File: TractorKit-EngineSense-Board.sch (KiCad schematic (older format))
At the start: 24 parts

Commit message: Final schematic
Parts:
- gave numbers to parts that had none: 24

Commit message: Final 2
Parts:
- added R10, R11, R12, R13, R9: 1k, Resistor_THT:R_Axial_DIN0207_L6.3mm_D2.5mm_P10.16mm_Horizontal, symbol Device:R
- added R4, R5, R6, R7, R8: 10k, Resistor_THT:R_Axial_DIN0207_L6.3mm_D2.5mm_P10.16mm_Horizontal, symbol Device:R
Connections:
- net +12V: now also J2.3 (Pin_3)
- net GND: now also R10.2, R11.2, R12.2, R13.2, R9.2
- net at J2.1 (Pin_1): now also R7.1
- net at J2.2 (Pin_2): now also R8.1
- net at J3.1 (Pin_1): now also R4.1
- net at J3.2 (Pin_2): now also R5.1
- net at J3.3 (Pin_3): now also R6.1
- net RX: now reaches J4.1 (Pin_1)
- net RX: now also U3.27 (IO16)
- net TX: now reaches J4.2 (Pin_2)
- net TX: now also U3.28 (IO17)
- net at U3.10 (IO25): now also R4.2, R9.1
- net at U3.11 (IO26): now also R10.1, R5.2
- net at U3.12 (IO27): now also R11.1, R6.2
- net at U3.7 (IO35): now also R13.1, R8.2
- net at U3.8 (IO32): now also R12.1, R7.2
- no-connect marks 8 -> 19
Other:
- note added: "12V WITH\nCURRENT\nSENSING"
- moved on the sheet: J2, J3, J4, J5

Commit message: First complete draft.
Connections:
- net ADC1_4: now reaches J2.1 (Pin_1), R7.1
- net ADC1_7: now reaches J2.2 (Pin_2), R8.1
- net ADC2_8: now reaches J3.1 (Pin_1), R4.1
- net ADC2_9: now reaches J3.2 (Pin_2), R5.1
- net ADC2_7: now reaches J3.3 (Pin_3), R6.1
- net 12VIN: now reaches J1.1 (Pin_1), JP1.2 (B), R1.1, U2.1 (IP+), U2.2 (IP+)
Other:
- moved on the sheet: R10, R11, R12, R13, R4, R5, R6, R7, R8, R9

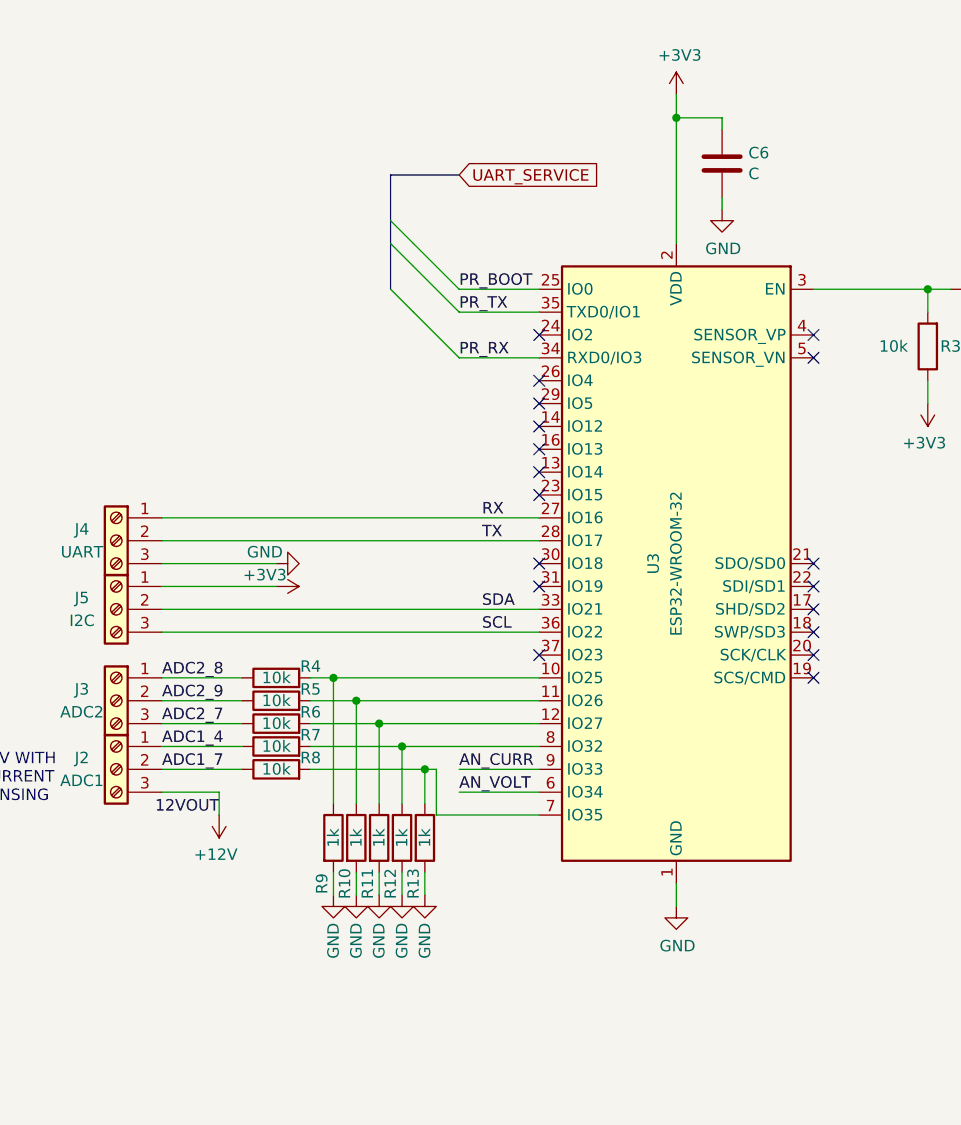
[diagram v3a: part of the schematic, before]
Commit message: Moved to SMD components
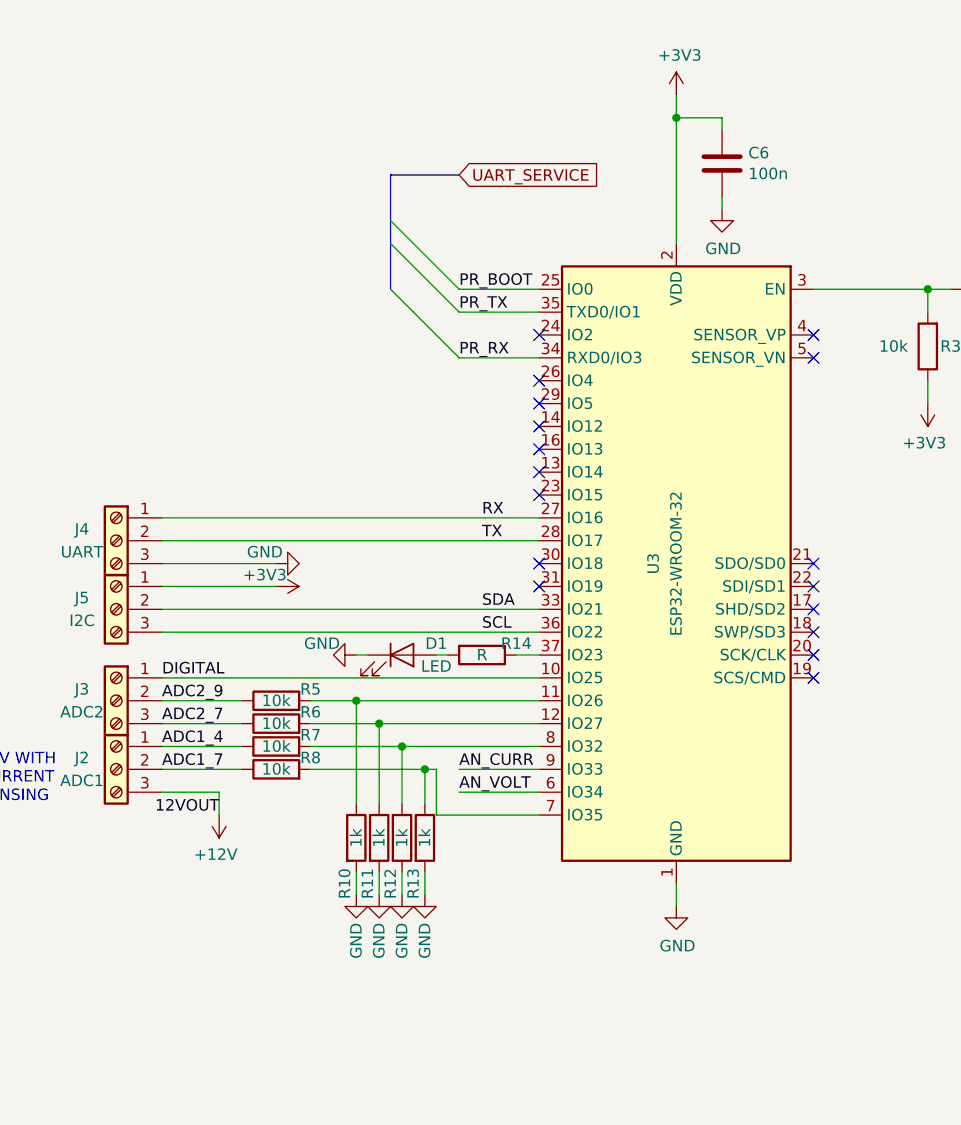
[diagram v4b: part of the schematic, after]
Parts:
- removed R4: 10k, Resistor_THT:R_Axial_DIN0207_L6.3mm_D2.5mm_P10.16mm_Horizontal, symbol Device:R
- removed R9: 1k, Resistor_THT:R_Axial_DIN0207_L6.3mm_D2.5mm_P10.16mm_Horizontal, symbol Device:R
- added D1: LED, LED_SMD:LED_0603_1608Metric_Pad1.05x0.95mm_HandSolder, symbol Device:LED
- added R14: R, Resistor_SMD:R_0603_1608Metric_Pad1.05x0.95mm_HandSolder, symbol Device:R
- C6: value C -> 100n
- R1, R10, R11, R12, R13, R2, R3, R5, R6, R7, R8: footprint Resistor_THT:R_Axial_DIN0207_L6.3mm_D2.5mm_P10.16mm_Horizontal -> Resistor_SMD:R_0603_1608Metric_Pad1.05x0.95mm_HandSolder
- TP1, TP2, TP3, TP4, TP5: footprint TestPoint:TestPoint_Pad_D1.5mm -> TestPoint:TestPoint_Pad_D1.0mm
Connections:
- net ADC2_8 is gone; now on net DIGITAL: J3.1 (Pin_1)
- net GND: now also D1.1 (K)
- net DIGITAL: now reaches U3.10 (IO25)
- net at U3.37 (IO23): now also R14.1
- new net: D1.2 (A), R14.2
- no-connect marks 19 -> 18
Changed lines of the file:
@@
 F 0 "TP5" V 2150 7150 50  0000 L CNN
 F 1 "SERVICE_GND" V 2150 7350 50  0000 L CNN
-F 2 "TestPoint:TestPoint_Pad_D1.5mm" H 2350 6950 50  0001 C CNN
+F 2 "TestPoint:TestPoint_Pad_D1.0mm" H 2350 6950 50  0001 C CNN
 F 3 "~" H 2350 6950 50  0001 C CNN
 	1    2150 6950
@@
 F 0 "TP3" V 2150 6950 50  0000 L CNN
 F 1 "SERVICE_RX" V 2150 7150 50  0000 L CNN
-F 2 "TestPoint:TestPoint_Pad_D1.5mm" H 2350 6750 50  0001 C CNN
+F 2 "TestPoint:TestPoint_Pad_D1.0mm" H 2350 6750 50  0001 C CNN
 F 3 "~" H 2350 6750 50  0001 C CNN
 	1    2150 6750
@@
 F 0 "TP2" V 2150 6850 50  0000 L CNN
 F 1 "SERVICE_TX" V 2150 7050 50  0000 L CNN
-F 2 "TestPoint:TestPoint_Pad_D1.5mm" H 2350 6650 50  0001 C CNN
+F 2 "TestPoint:TestPoint_Pad_D1.0mm" H 2350 6650 50  0001 C CNN
 F 3 "~" H 2350 6650 50  0001 C CNN
 	1    2150 6650
@@
 F 0 "TP1" V 2150 6750 50  0000 L CNN
 F 1 "SERVICE_BOOT" V 2150 6950 50  0000 L CNN
-F 2 "TestPoint:TestPoint_Pad_D1.5mm" H 2350 6550 50  0001 C CNN
+F 2 "TestPoint:TestPoint_Pad_D1.0mm" H 2350 6550 50  0001 C CNN
 F 3 "~" H 2350 6550 50  0001 C CNN
 	1    2150 6550
@@
 P 8700 2450
 F 0 "C6" H 8815 2496 50  0000 L CNN
-F 1 "C" H 8815 2405 50  0000 L CNN
+F 1 "100n" H 8815 2405 50  0000 L CNN
 F 2 "Capacitor_THT:C_Disc_D4.7mm_W2.5mm_P5.00mm" H 8738 2300 50  0001 C CNN
 F 3 "~" H 8700 2450 50  0001 C CNN
@@
 F 0 "TP4" V 2150 7050 50  0000 L CNN
 F 1 "SERVICE_3V3" V 2150 7250 50  0000 L CNN
-F 2 "TestPoint:TestPoint_Pad_D1.5mm" H 2350 6850 50  0001 C CNN
+F 2 "TestPoint:TestPoint_Pad_D1.0mm" H 2350 6850 50  0001 C CNN
 F 3 "~" H 2350 6850 50  0001 C CNN
 	1    2150 6850
@@
 F 0 "R1" V 2350 4900 50  0000 C CNN
 F 1 "10k" V 2250 4900 50  0000 C CNN
-F 2 "Resistor_THT:R_Axial_DIN0207_L6.3mm_D2.5mm_P10.16mm_Horizontal" V 2380 4900 50  0001 C CNN
+F 2 "Resistor_SMD:R_0603_1608Metric_Pad1.05x0.95mm_HandSolder" V 2380 4900 50  0001 C CNN
 F 3 "~" H 2450 4900 50  0001 C CNN
 	1    2450 4900
@@
 F 0 "R2" V 2850 4900 50  0000 C CNN
 F 1 "1k" V 2750 4900 50  0000 C CNN
-F 2 "Resistor_THT:R_Axial_DIN0207_L6.3mm_D2.5mm_P10.16mm_Horizontal" V 2880 4900 50  0001 C CNN
+F 2 "Resistor_SMD:R_0603_1608Metric_Pad1.05x0.95mm_HandSolder" V 2880 4900 50  0001 C CNN
 F 3 "~" H 2950 4900 50  0001 C CNN
 	1    2950 4900
@@
 F 0 "R3" H 9500 3250 50  0000 C CNN
 F 1 "10k" H 9750 3250 50  0000 C CNN
-F 2 "Resistor_THT:R_Axial_DIN0207_L6.3mm_D2.5mm_P10.16mm_Horizontal" V 9530 3250 50  0001 C CNN
+F 2 "Resistor_SMD:R_0603_1608Metric_Pad1.05x0.95mm_HandSolder" V 9530 3250 50  0001 C CNN
 F 3 "~" H 9600 3250 50  0001 C CNN
 	1    9600 3250
@@
 F 0 "R8" V 6800 4950 50  0000 C CNN
 F 1 "10k" V 6750 5100 50  0000 C CNN
-F 2 "Resistor_THT:R_Axial_DIN0207_L6.3mm_D2.5mm_P10.16mm_Horizontal" V 6680 5100 50  0001 C CNN
+F 2 "Resistor_SMD:R_0603_1608Metric_Pad1.05x0.95mm_HandSolder" V 6680 5100 50  0001 C CNN
 F 3 "~" H 6750 5100 50  0001 C CNN
 	1    6750 5100
@@
 F 0 "R7" V 6800 4850 50  0000 C CNN
 F 1 "10k" V 6750 5000 50  0000 C CNN
-F 2 "Resistor_THT:R_Axial_DIN0207_L6.3mm_D2.5mm_P10.16mm_Horizontal" V 6680 5000 50  0001 C CNN
+F 2 "Resistor_SMD:R_0603_1608Metric_Pad1.05x0.95mm_HandSolder" V 6680 5000 50  0001 C CNN
 F 3 "~" H 6750 5000 50  0001 C CNN
 	1    6750 5000
@@
 F 0 "R6" V 6800 4750 50  0000 C CNN
 F 1 "10k" V 6750 4900 50  0000 C CNN
-F 2 "Resistor_THT:R_Axial_DIN0207_L6.3mm_D2.5mm_P10.16mm_Horizontal" V 6680 4900 50  0001 C CNN
+F 2 "Resistor_SMD:R_0603_1608Metric_Pad1.05x0.95mm_HandSolder" V 6680 4900 50  0001 C CNN
 F 3 "~" H 6750 4900 50  0001 C CNN
 	1    6750 4900
@@
 F 0 "R5" V 6800 4650 50  0000 C CNN
 F 1 "10k" V 6750 4800 50  0000 C CNN
-F 2 "Resistor_THT:R_Axial_DIN0207_L6.3mm_D2.5mm_P10.16mm_Horizontal" V 6680 4800 50  0001 C CNN
+F 2 "Resistor_SMD:R_0603_1608Metric_Pad1.05x0.95mm_HandSolder" V 6680 4800 50  0001 C CNN
 F 3 "~" H 6750 4800 50  0001 C CNN
 	1    6750 4800
@@
 Wire Wire Line
 	6600 4800 6250 4800
-$Comp
-L Device:R R?
-U 1 1 5F1F4248
-P 6750 4700
-AR Path="/5F193498/5F1F4248" Ref="R?"  Part="1"
-AR Path="/5F1F4248" Ref="R4"  Part="1"
-F 0 "R4" V 6800 4550 50  0000 C CNN
-F 1 "10k" V 6750 4700 50  0000 C CNN
-F 2 "Resistor_THT:R_Axial_DIN0207_L6.3mm_D2.5mm_P10.16mm_Horizontal" V 6680 4700 50  0001 C CNN
-F 3 "~" H 6750 4700 50  0001 C CNN
-	1    6750 4700
-	0    -1   -1   0
-$EndComp
-Wire Wire Line
-	6600 4700 6250 4700
-$Comp
-L power:GND #PWR023
-U 1 1 5F1D06E4
-P 7000 5650
-F 0 "#PWR023" H 7000 5400 50  0001 C CNN
-F 1 "GND" V 7000 5450 50  0000 C CNN
-F 2 "" H 7000 5650 50  0001 C CNN
-F 3 "" H 7000 5650 50  0001 C CNN
-	1    7000 5650
-	1    0    0    -1
-$EndComp
 $Comp
 L Device:R R10
@@
 F 0 "R10" V 7050 5200 50  0000 C CNN
 F 1 "1k" V 7100 5400 50  0000 C CNN
-F 2 "Resistor_THT:R_Axial_DIN0207_L6.3mm_D2.5mm_P10.16mm_Horizontal" V 7030 5400 50  0001 C CNN
+F 2 "Resistor_SMD:R_0603_1608Metric_Pad1.05x0.95mm_HandSolder" V 7030 5400 50  0001 C CNN
 F 3 "~" H 7100 5400 50  0001 C CNN
 	1    7100 5400
@@
 F 0 "R11" V 7150 5200 50  0000 C CNN
 F 1 "1k" V 7200 5400 50  0000 C CNN
-F 2 "Resistor_THT:R_Axial_DIN0207_L6.3mm_D2.5mm_P10.16mm_Horizontal" V 7130 5400 50  0001 C CNN
+F 2 "Resistor_SMD:R_0603_1608Metric_Pad1.05x0.95mm_HandSolder" V 7130 5400 50  0001 C CNN
 F 3 "~" H 7200 5400 50  0001 C CNN
 	1    7200 5400
@@
 F 0 "R12" V 7250 5200 50  0000 C CNN
 F 1 "1k" V 7300 5400 50  0000 C CNN
-F 2 "Resistor_THT:R_Axial_DIN0207_L6.3mm_D2.5mm_P10.16mm_Horizontal" V 7230 5400 50  0001 C CNN
+F 2 "Resistor_SMD:R_0603_1608Metric_Pad1.05x0.95mm_HandSolder" V 7230 5400 50  0001 C CNN
 F 3 "~" H 7300 5400 50  0001 C CNN
 	1    7300 5400
@@
 F 0 "R13" V 7350 5200 50  0000 C CNN
 F 1 "1k" V 7400 5400 50  0000 C CNN
-F 2 "Resistor_THT:R_Axial_DIN0207_L6.3mm_D2.5mm_P10.16mm_Horizontal" V 7330 5400 50  0001 C CNN
+F 2 "Resistor_SMD:R_0603_1608Metric_Pad1.05x0.95mm_HandSolder" V 7330 5400 50  0001 C CNN
 F 3 "~" H 7400 5400 50  0001 C CNN
 	1    7400 5400
@@
 Wire Wire Line
 	7100 4800 7100 5250
-Wire Wire Line
-	7000 5250 7000 4700
-Wire Wire Line
-	7000 5650 7000 5550
-$Comp
-L Device:R R9
-U 1 1 5F1D06DD
-P 7000 5400
-F 0 "R9" V 6950 5200 50  0000 C CNN
-F 1 "1k" V 7000 5400 50  0000 C CNN
-F 2 "Resistor_THT:R_Axial_DIN0207_L6.3mm_D2.5mm_P10.16mm_Horizontal" V 6930 5400 50  0001 C CNN
-F 3 "~" H 7000 5400 50  0001 C CNN
-	1    7000 5400
-	1    0    0    -1
-$EndComp
 NoConn ~ 7900 3200
 NoConn ~ 7900 3400
@@
 NoConn ~ 7900 4200
 NoConn ~ 7900 4300
-NoConn ~ 7900 4600
 NoConn ~ 2400 3700
 Text Label 1450 4700 0    50   ~ 0
@@
 Text Label 6500 5300 2    50   ~ 0
 12VOUT
-Connection ~ 7000 4700
-Wire Wire Line
-	7000 4700 7900 4700
 Connection ~ 7100 4800
 Wire Wire Line
@@
 Wire Wire Line
 	6900 4800 7100 4800
-Wire Wire Line
-	6900 4700 7000 4700
-Wire Bus Line
-	2600 6250 2600 6650
-Wire Bus Line
-	7250 2500 7250 3000
 Text Label 6250 4700 0    50   ~ 0
-ADC2_8
+DIGITAL
 Text Label 6250 4800 0    50   ~ 0
 ADC2_9
@@
 Text Label 6250 5100 0    50   ~ 0
 ADC1_7
+$Comp
+L Device:R R14
+U 1 1 5F21F512
+P 7650 4600
+F 0 "R14" V 7600 4750 50  0000 C CNN
+F 1 "R" V 7650 4600 50  0000 C CNN
+F 2 "Resistor_SMD:R_0603_1608Metric_Pad1.05x0.95mm_HandSolder" V 7580 4600 50  0001 C CNN
+F 3 "~" H 7650 4600 50  0001 C CNN
+	1    7650 4600
+	0    1    1    0
+$EndComp
+Wire Wire Line
+	7800 4600 7900 4600
+$Comp
+L Device:LED D1
+U 1 1 5F22314C
+P 7300 4600
+F 0 "D1" H 7450 4650 50  0000 C CNN
+F 1 "LED" H 7450 4550 50  0000 C CNN
+F 2 "LED_SMD:LED_0603_1608Metric_Pad1.05x0.95mm_HandSolder" H 7300 4600 50  0001 C CNN
+F 3 "~" H 7300 4600 50  0001 C CNN
+	1    7300 4600
+	1    0    0    -1
+$EndComp
+$Comp
+L power:GND #PWR0101
+U 1 1 5F226B49
+P 7100 4600
+F 0 "#PWR0101" H 7100 4350 50  0001 C CNN
+F 1 "GND" V 7050 4450 50  0000 C CNN
+F 2 "" H 7100 4600 50  0001 C CNN
+F 3 "" H 7100 4600 50  0001 C CNN
+	1    7100 4600
+	0    1    1    0
+$EndComp
+Wire Wire Line
+	7450 4600 7500 4600
+Wire Wire Line
+	7150 4600 7100 4600
+Wire Wire Line
+	6250 4700 7900 4700
+Wire Bus Line
+	2600 6250 2600 6650
+Wire Bus Line
+	7250 2500 7250 3000
 $EndSCHEMATC
